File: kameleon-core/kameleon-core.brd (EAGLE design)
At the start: 21 x 38 mm, 39 parts, among them CN1 USB, CN3 LEFT, CN4 RIGHT, CN5 SWD, IC3 STM32F411CE/UFQFPN48, IC4 AP2112K-3.3TRG1, SW1 NRST, SW2 BTN, Y1 8MHz

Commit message: Change R10 value to 10K
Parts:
- R10: value 100K -> 10K
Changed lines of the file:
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@@
 <attribute name="NAME" x="6.35" y="6.50875" size="0.4064" layer="25" rot="R180" align="center"/>
 </element>
-<element name="R10" library="Kameleon" package="1608" value="100K" x="16.51" y="22.86" smashed="yes" rot="R270">
+<element name="R10" library="Kameleon" package="1608" value="10K" x="16.51" y="22.86" smashed="yes" rot="R270">
 <attribute name="NAME" x="16.51" y="22.86" size="0.4064" layer="25" align="center"/>
 </element>

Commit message: Remove R3 and R6 because it's not needed
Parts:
- removed R3: 10K, Kameleon:1608
- removed R6: 1K, Kameleon:1608
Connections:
- removed net N$1: IC3.44, R6.2
- removed net N$2: IC3.20, R3.2
- net BOOT0: now also IC3.44; no longer R6.1
- net GND: now also IC3.20; no longer R3.1
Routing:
- net BOOT0: track 8.93 -> 24.5 mm, vias 0 -> 2
- net N$1: track 15.0 -> 0.00 mm, vias 2 -> 0
- net GND: track 7.46 -> 11.0 mm
- net N$2: track 2.06 -> 0.00 mm

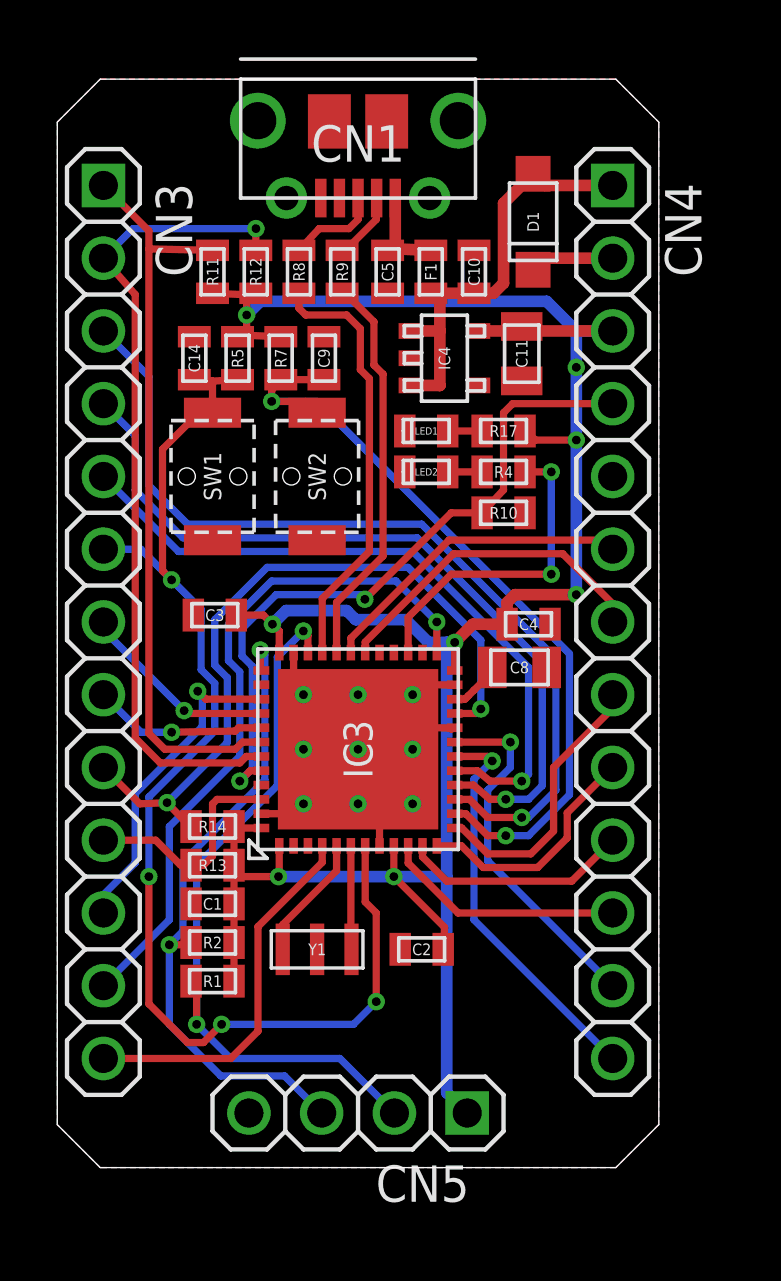
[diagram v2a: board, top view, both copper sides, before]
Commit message: Change CN3 and CN4 from Top to Bottom.  - Resolve the issue #3
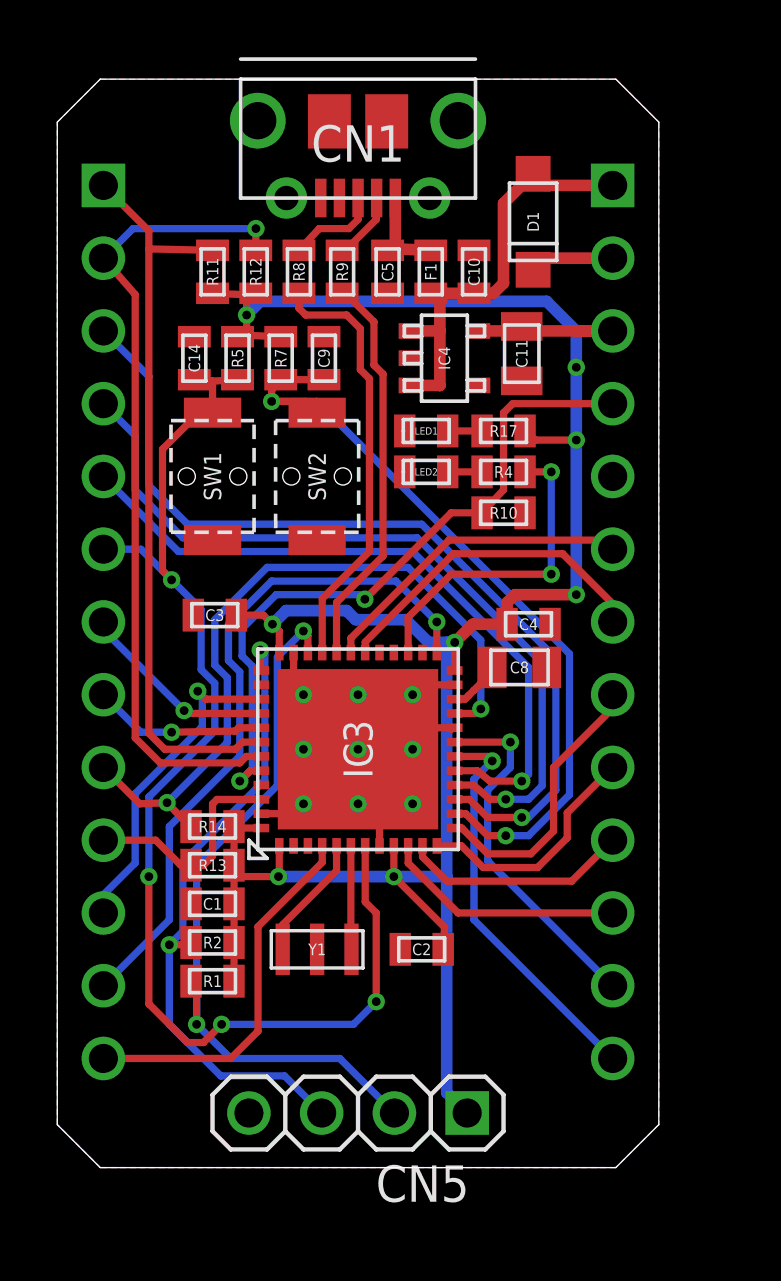
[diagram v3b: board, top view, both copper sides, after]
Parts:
- flipped CN3 to the bottom
- flipped CN4 to the bottom
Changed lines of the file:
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@@
 <attribute name="NAME" x="11.43" y="35.755" size="1.27" layer="25" align="center"/>
 </element>
-<element name="CN3" library="Kameleon" package="1X13" value="LEFT" x="2.54" y="19.05" smashed="yes" rot="R270">
-<attribute name="NAME" x="4.3688" y="34.3662" size="1.27" layer="25" ratio="10" rot="R270"/>
-<attribute name="VALUE" x="-0.635" y="34.29" size="1.27" layer="27" rot="R270"/>
-</element>
-<element name="CN4" library="Kameleon" package="1X13" value="RIGHT" x="20.32" y="19.05" smashed="yes" rot="R270">
-<attribute name="NAME" x="22.1488" y="34.3662" size="1.27" layer="25" ratio="10" rot="R270"/>
-<attribute name="VALUE" x="17.145" y="34.29" size="1.27" layer="27" rot="R270"/>
+<element name="CN3" library="Kameleon" package="1X13" value="LEFT" x="2.54" y="19.05" smashed="yes" rot="MR270">
+<attribute name="NAME" x="0.7112" y="34.3662" size="1.27" layer="26" ratio="10" rot="MR270"/>
+<attribute name="VALUE" x="5.715" y="34.29" size="1.27" layer="28" rot="MR270"/>
+</element>
+<element name="CN4" library="Kameleon" package="1X13" value="RIGHT" x="20.32" y="19.05" smashed="yes" rot="MR270">
+<attribute name="NAME" x="18.4912" y="34.3662" size="1.27" layer="26" ratio="10" rot="MR270"/>
+<attribute name="VALUE" x="23.495" y="34.29" size="1.27" layer="28" rot="MR270"/>
 </element>
 <element name="CN5" library="Kameleon" package="1X04" value="SWD" x="11.43" y="1.905" smashed="yes" rot="R180">
@@
 <wire x1="8.918125" y1="19.446875" x2="11.033125" y2="19.446875" width="0.4064" layer="16"/>
 <wire x1="19.05" y1="27.94" x2="19.05" y2="29.21" width="0.4064" layer="16"/>
-<wire x1="19.05" y1="29.21" x2="20.32" y2="29.21" width="0.4064" layer="16"/>
+<wire x1="19.05" y1="29.21" x2="20.32" y2="29.21" width="0.4064" layer="1"/>
 <wire x1="12.68" y1="10.16" x2="14.525625" y2="10.16" width="0.4064" layer="16"/>
 <wire x1="14.525625" y1="10.16" x2="14.525625" y2="2.619375" width="0.4064" layer="16"/>

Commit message: I2C pull-ups are changed from 10K to NC
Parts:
- R11, R12, R13, R14: value 10K -> NC
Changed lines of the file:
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@@
 <attribute name="NAME" x="16.51" y="22.86" size="0.4064" layer="25" align="center"/>
 </element>
-<element name="R11" library="Kameleon" package="1608" value="10K" x="6.35" y="31.27375" smashed="yes">
+<element name="R11" library="Kameleon" package="1608" value="NC" x="6.35" y="31.27375" smashed="yes">
 <attribute name="NAME" x="6.35" y="31.27375" size="0.4064" layer="25" rot="R90" align="center"/>
 </element>
-<element name="R12" library="Kameleon" package="1608" value="10K" x="7.858125" y="31.27375" smashed="yes">
+<element name="R12" library="Kameleon" package="1608" value="NC" x="7.858125" y="31.27375" smashed="yes">
 <attribute name="NAME" x="7.858125" y="31.27375" size="0.4064" layer="25" rot="R90" align="center"/>
 </element>
-<element name="R13" library="Kameleon" package="1608" value="10K" x="6.35" y="10.556875" smashed="yes" rot="R90">
+<element name="R13" library="Kameleon" package="1608" value="NC" x="6.35" y="10.556875" smashed="yes" rot="R90">
 <attribute name="NAME" x="6.35" y="10.556875" size="0.4064" layer="25" rot="R180" align="center"/>
 </element>
-<element name="R14" library="Kameleon" package="1608" value="10K" x="6.35" y="11.90625" smashed="yes" rot="R90">
+<element name="R14" library="Kameleon" package="1608" value="NC" x="6.35" y="11.90625" smashed="yes" rot="R90">
 <attribute name="NAME" x="6.35" y="11.90625" size="0.4064" layer="25" rot="R180" align="center"/>
 </element>
